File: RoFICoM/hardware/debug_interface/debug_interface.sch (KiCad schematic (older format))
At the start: 5 parts, among them J4 RoFICoM

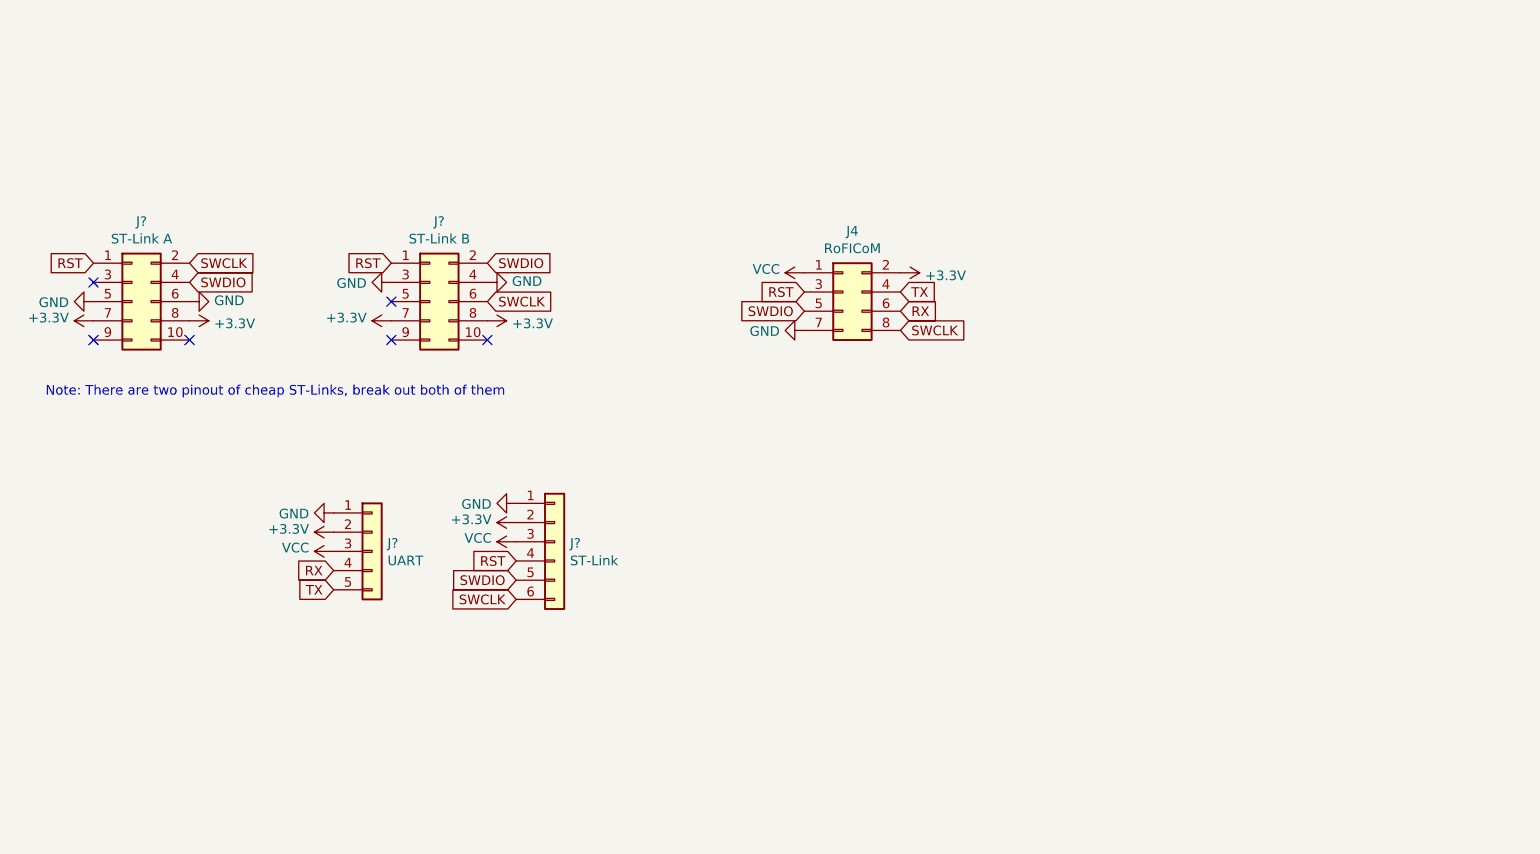
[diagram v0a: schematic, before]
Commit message: RoFICoM: Rework debug interface into v0.2
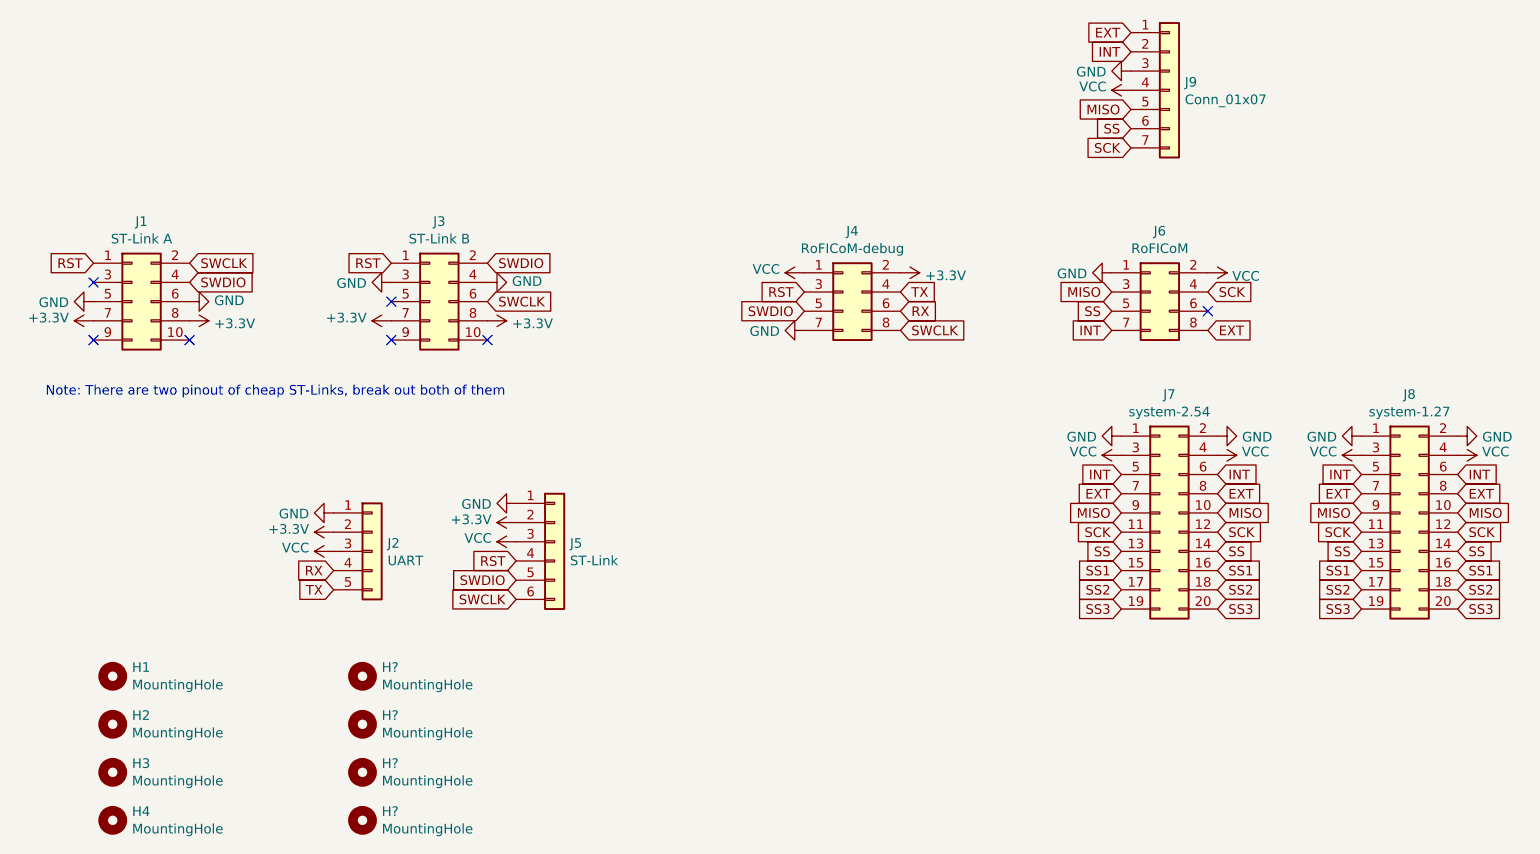
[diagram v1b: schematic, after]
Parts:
- added H1, H2, H3, H4: MountingHole, rofi:ThreadedHole-M2, symbol Mechanical:MountingHole
- added H? (x4): MountingHole, MountingHole:MountingHole_2.2mm_M2, symbol Mechanical:MountingHole
- added J6: RoFICoM, rofi:molex-505004-0812, symbol Connector_Generic:Conn_02x04_Odd_Even
- added J7: system-2.54, Connector_PinHeader_2.54mm:PinHeader_2x10_P2.54mm_Vertical, symbol Connector_Generic:Conn_02x10_Odd_Even
- added J8: system-1.27, Connector_PinHeader_1.27mm:PinHeader_2x10_P1.27mm_Vertical, symbol Connector_Generic:Conn_02x10_Odd_Even
- added J9: Conn_01x07, rofi:pogo_pads_4_3, symbol Connector_Generic:Conn_01x07
- J1, J3: renamed from J?; footprint Connector_PinSocket_2.54mm:PinSocket_2x05_P2.54mm_Vertical -> Connector_IDC:IDC-Header_2x05_P2.54mm_Vertical
- J4: value RoFICoM -> RoFICoM-debug
- gave numbers to parts that had none: 2
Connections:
- net GND: now also J6.1 (Pin_1), J7.1 (Pin_1), J7.2 (Pin_2), J8.1 (Pin_1), J8.2 (Pin_2), J9.3 (Pin_3)
- net VCC: now also J6.2 (Pin_2), J7.3 (Pin_3), J7.4 (Pin_4), J8.3 (Pin_3), J8.4 (Pin_4), J9.4 (Pin_4)
- new net EXT: J6.8 (Pin_8), J7.7 (Pin_7), J7.8 (Pin_8), J8.7 (Pin_7), J8.8 (Pin_8), J9.1 (Pin_1)
- new net INT: J6.7 (Pin_7), J7.5 (Pin_5), J7.6 (Pin_6), J8.5 (Pin_5), J8.6 (Pin_6), J9.2 (Pin_2)
- new net MISO: J6.3 (Pin_3), J7.10 (Pin_10), J7.9 (Pin_9), J8.10 (Pin_10), J8.9 (Pin_9), J9.5 (Pin_5)
- new net SCK: J6.4 (Pin_4), J7.11 (Pin_11), J7.12 (Pin_12), J8.11 (Pin_11), J8.12 (Pin_12), J9.7 (Pin_7)
- new net SS: J6.5 (Pin_5), J7.13 (Pin_13), J7.14 (Pin_14), J8.13 (Pin_13), J8.14 (Pin_14), J9.6 (Pin_6)
- new net SS1: J7.15 (Pin_15), J7.16 (Pin_16), J8.15 (Pin_15), J8.16 (Pin_16)
- new net SS2: J7.17 (Pin_17), J7.18 (Pin_18), J8.17 (Pin_17), J8.18 (Pin_18)
- new net SS3: J7.19 (Pin_19), J7.20 (Pin_20), J8.19 (Pin_19), J8.20 (Pin_20)
- no-connect marks 6 -> 7
